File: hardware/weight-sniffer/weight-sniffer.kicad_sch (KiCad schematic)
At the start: 8 parts, among them J1 LOAD_CELL_CONNECTOR, SW1 SEND_BTN, U1 ESP32-DEVKIT-V1, U2 SEN-13879

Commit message: footprint assignment
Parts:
- BZ1: footprint (none) -> Buzzer_Beeper:Buzzer_D14mm_H7mm_P10mm
- D1: footprint (none) -> LED_THT:LED_D3.0mm
- J1: footprint (none) -> Connector_PinHeader_2.54mm:PinHeader_1x04_P2.54mm_Vertical
- R1, R2: footprint (none) -> Resistor_THT:R_Axial_DIN0204_L3.6mm_D1.6mm_P7.62mm_Horizontal
- SW1: footprint (none) -> Connector_PinHeader_2.54mm:PinHeader_1x02_P2.54mm_Vertical
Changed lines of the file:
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@@
 			)
 		)
-		(property "Footprint" ""
+		(property "Footprint" "Resistor_THT:R_Axial_DIN0204_L3.6mm_D1.6mm_P7.62mm_Horizontal"
 			(at 93.98 59.69 0)
 			(effects
@@
 			)
 		)
-		(property "Footprint" ""
+		(property "Footprint" "LED_THT:LED_D3.0mm"
 			(at 93.98 52.07 0)
 			(effects
@@
 			)
 		)
-		(property "Footprint" ""
+		(property "Footprint" "Connector_PinHeader_2.54mm:PinHeader_1x04_P2.54mm_Vertical"
 			(at 179.07 135.89 0)
 			(effects
@@
 			)
 		)
-		(property "Footprint" ""
+		(property "Footprint" "Resistor_THT:R_Axial_DIN0204_L3.6mm_D1.6mm_P7.62mm_Horizontal"
 			(at 109.22 80.01 0)
 			(effects
@@
 			)
 		)
-		(property "Footprint" ""
+		(property "Footprint" "Buzzer_Beeper:Buzzer_D14mm_H7mm_P10mm"
 			(at 173.355 77.47 90)
 			(effects
@@
 			)
 		)
-		(property "Footprint" ""
+		(property "Footprint" "Connector_PinHeader_2.54mm:PinHeader_1x02_P2.54mm_Vertical"
 			(at 99.06 85.09 0)
 			(effects

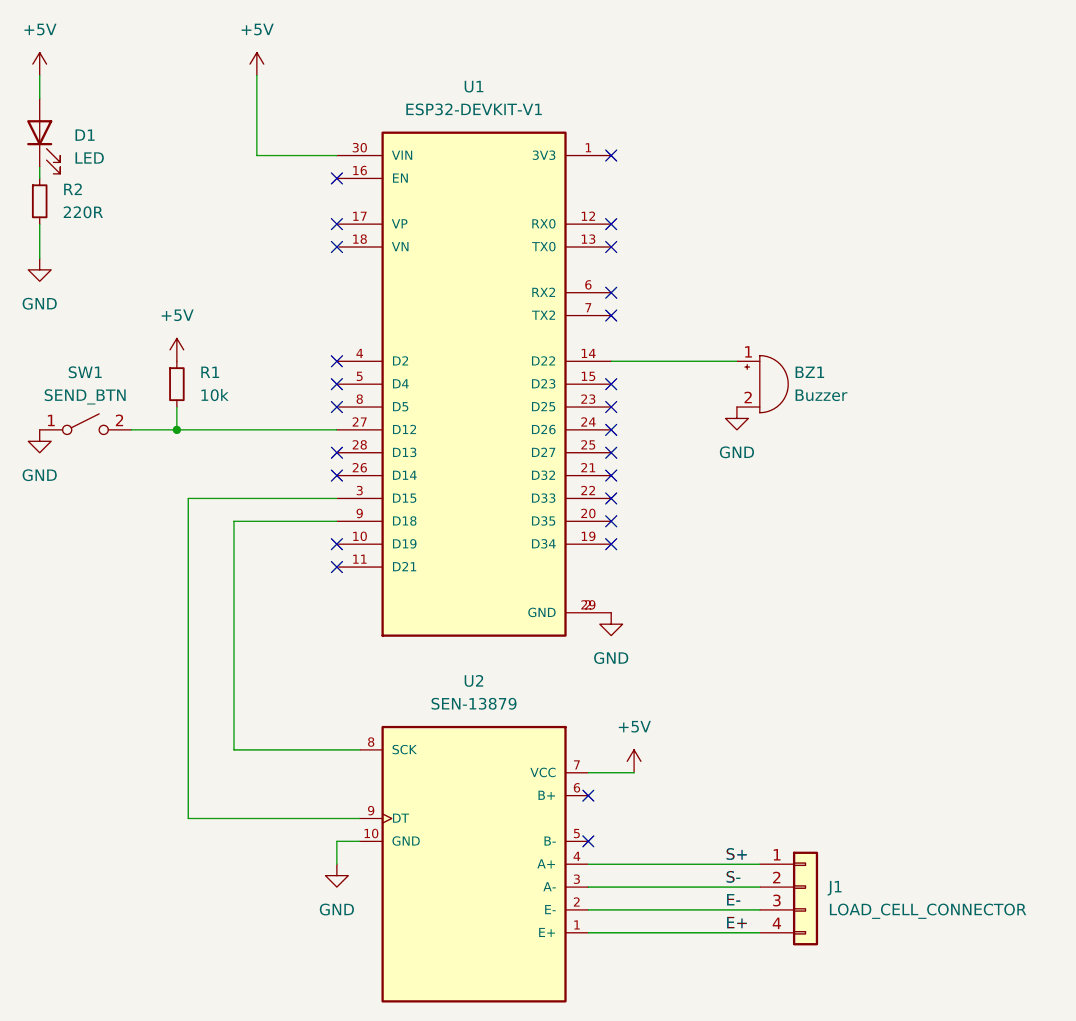
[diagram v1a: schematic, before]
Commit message: adds routed tracks
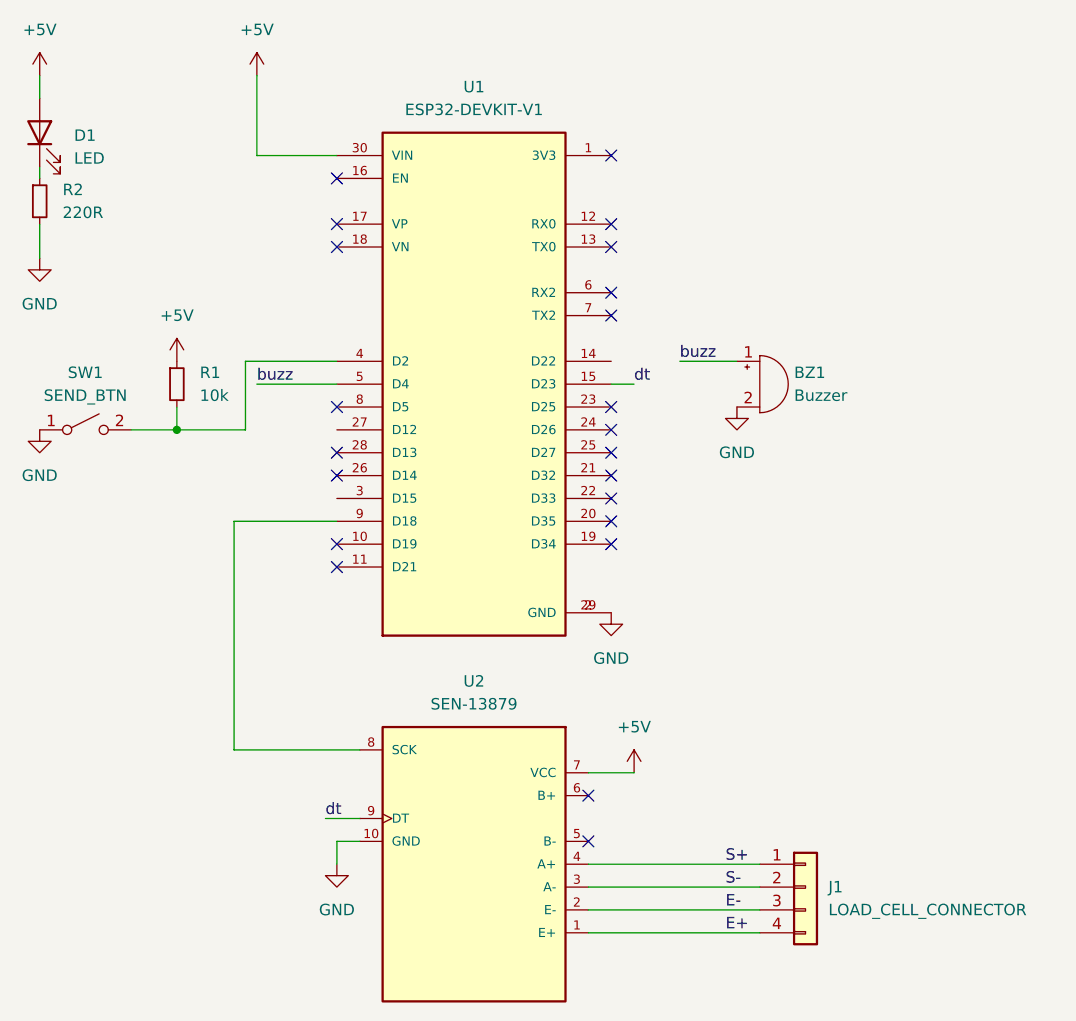
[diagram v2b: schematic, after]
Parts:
- U2: footprint SEN-13879:SPARKFUN_SEN-13879 -> HX711-MODULE:SPARKFUN_SEN-13879
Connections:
- net at U1.14 (D22): no longer BZ1.1 (+)
- net dt: now reaches U1.15 (D23)
- net dt: now also U2.9 (DT)
- net at R1.2, SW1.2 (B): now also U1.4 (D2); no longer U1.27 (D12)
- net at U1.3 (D15): no longer U2.9 (DT)
- net buzz: now reaches U1.5 (D4)
- net buzz: now also BZ1.1 (+)
- no-connect marks 25 -> 22
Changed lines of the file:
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@@
-	)
-	(no_connect
-		(at 127 77.47)
-	)
-	(no_connect
-		(at 127 80.01)
 	)
 	(no_connect
@@
 	)
 	(no_connect
-		(at 157.48 80.01)
-	)
-	(no_connect
 		(at 127 62.23)
 	)
@@
 	(wire
 		(pts
-			(xy 110.49 92.71) (xy 127 92.71)
-		)
-		(stroke
-			(width 0)
-			(type default)
-		)
-	)
-	(wire
-		(pts
-			(xy 157.48 77.47) (xy 171.45 77.47)
+			(xy 116.84 85.09) (xy 116.84 77.47)
+		)
+		(stroke
+			(width 0)
+			(type default)
+		)
+	)
+	(wire
+		(pts
+			(xy 116.84 77.47) (xy 127 77.47)
+		)
+		(stroke
+			(width 0)
+			(type default)
+		)
+	)
+	(wire
+		(pts
+			(xy 125.73 128.27) (xy 129.54 128.27)
+		)
+		(stroke
+			(width 0)
+			(type default)
+		)
+	)
+	(wire
+		(pts
+			(xy 160.02 80.01) (xy 157.48 80.01)
 		)
 		(stroke
@@
 	(wire
 		(pts
-			(xy 110.49 128.27) (xy 110.49 92.71)
-		)
-		(stroke
-			(width 0)
-			(type default)
-		)
-	)
-	(wire
-		(pts
-			(xy 129.54 128.27) (xy 110.49 128.27)
-		)
-		(stroke
-			(width 0)
-			(type default)
-		)
-	)
-	(wire
-		(pts
 			(xy 154.94 133.35) (xy 173.99 133.35)
 		)
@@
 	(wire
 		(pts
-			(xy 109.22 85.09) (xy 127 85.09)
-		)
-		(stroke
-			(width 0)
-			(type default)
-		)
-	)
-	(wire
-		(pts
 			(xy 127 54.61) (xy 118.11 54.61)
 		)
@@
 	(wire
 		(pts
+			(xy 165.1 77.47) (xy 171.45 77.47)
+		)
+		(stroke
+			(width 0)
+			(type default)
+		)
+	)
+	(wire
+		(pts
+			(xy 109.22 85.09) (xy 116.84 85.09)
+		)
+		(stroke
+			(width 0)
+			(type default)
+		)
+	)
+	(wire
+		(pts
+			(xy 118.11 80.01) (xy 127 80.01)
+		)
+		(stroke
+			(width 0)
+			(type default)
+		)
+	)
+	(wire
+		(pts
 			(xy 154.94 138.43) (xy 173.99 138.43)
 		)
@@
 		)
 	)
-	(label "E+"
-		(at 170.18 140.97 0)
+	(label "dt"
+		(at 160.02 80.01 0)
 		(fields_autoplaced yes)
 		(effects
@@
 		)
 	)
-	(label "S+"
-		(at 170.18 133.35 0)
+	(label "E+"
+		(at 170.18 140.97 0)
 		(fields_autoplaced yes)
 		(effects
@@
 		)
 	)
-	(label "S-"
-		(at 170.18 135.89 0)
+	(label "buzz"
+		(at 165.1 77.47 0)
 		(fields_autoplaced yes)
 		(effects
@@
 		)
 	)
+	(label "S+"
+		(at 170.18 133.35 0)
+		(fields_autoplaced yes)
+		(effects
+			(font
+				(size 1.27 1.27)
+			)
+			(justify left bottom)
+		)
+	)
+	(label "buzz"
+		(at 118.11 80.01 0)
+		(fields_autoplaced yes)
+		(effects
+			(font
+				(size 1.27 1.27)
+			)
+			(justify left bottom)
+		)
+	)
+	(label "S-"
+		(at 170.18 135.89 0)
+		(fields_autoplaced yes)
+		(effects
+			(font
+				(size 1.27 1.27)
+			)
+			(justify left bottom)
+		)
+	)
 	(label "E-"
 		(at 170.18 138.43 0)
+		(fields_autoplaced yes)
+		(effects
+			(font
+				(size 1.27 1.27)
+			)
+			(justify left bottom)
+		)
+	)
+	(label "dt"
+		(at 125.73 128.27 0)
 		(fields_autoplaced yes)
 		(effects
@@
 			)
 		)
-		(property "Footprint" "SEN-13879:SPARKFUN_SEN-13879"
+		(property "Footprint" "HX711-MODULE:SPARKFUN_SEN-13879"
 			(at 142.24 149.098 0)
 			(effects
